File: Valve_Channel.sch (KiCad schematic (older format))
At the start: 12 parts, among them Q1 MMBT3904, Q2 Q_PMOS_GDS, U3 INA181AX

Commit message: added jtag programming header for uC
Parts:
- U3: symbol sternie:INA181AX -> bangbang_rev1-rescue:INA181AX-sternie
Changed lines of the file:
@@
 EESchema Schematic File Version 4
-LIBS:bangbang_rev1-cache
 EELAYER 30 0
 EELAYER END
@@
 $EndComp
 $Comp
-L sternie:INA181AX U3
+L bangbang_rev1-rescue:INA181AX-sternie U3
 U 1 1 59699268
 P 4750 4575

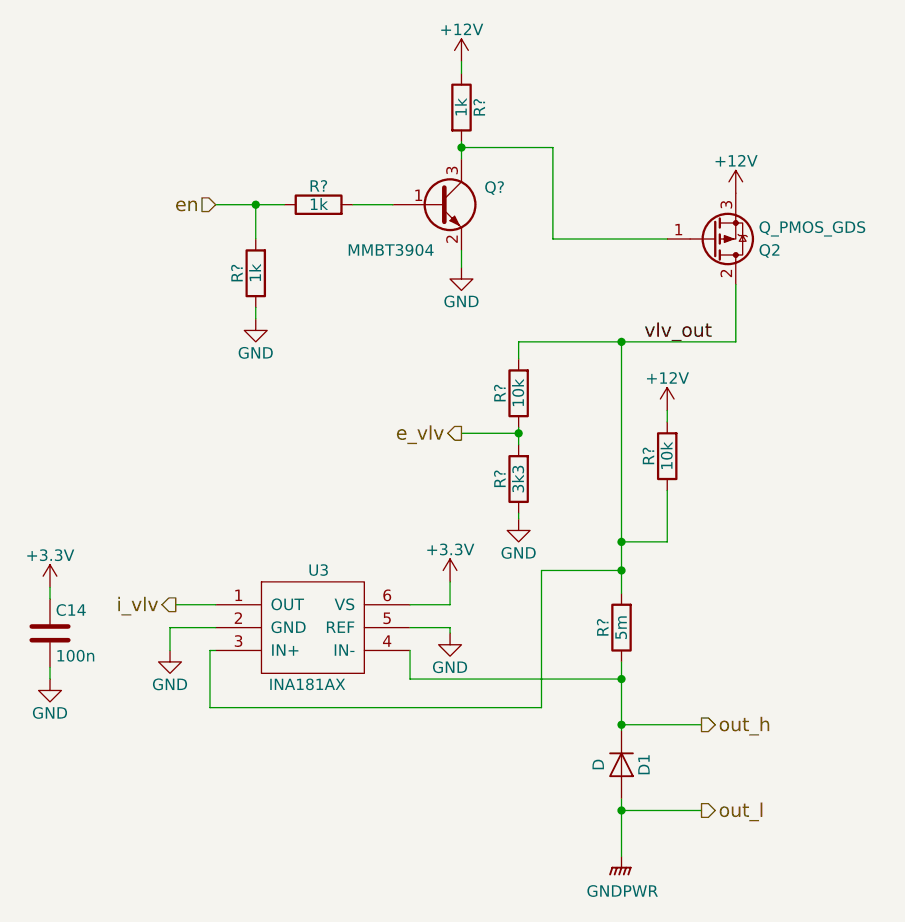
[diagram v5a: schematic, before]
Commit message: Eletrical Rules Check
Fixed some label names
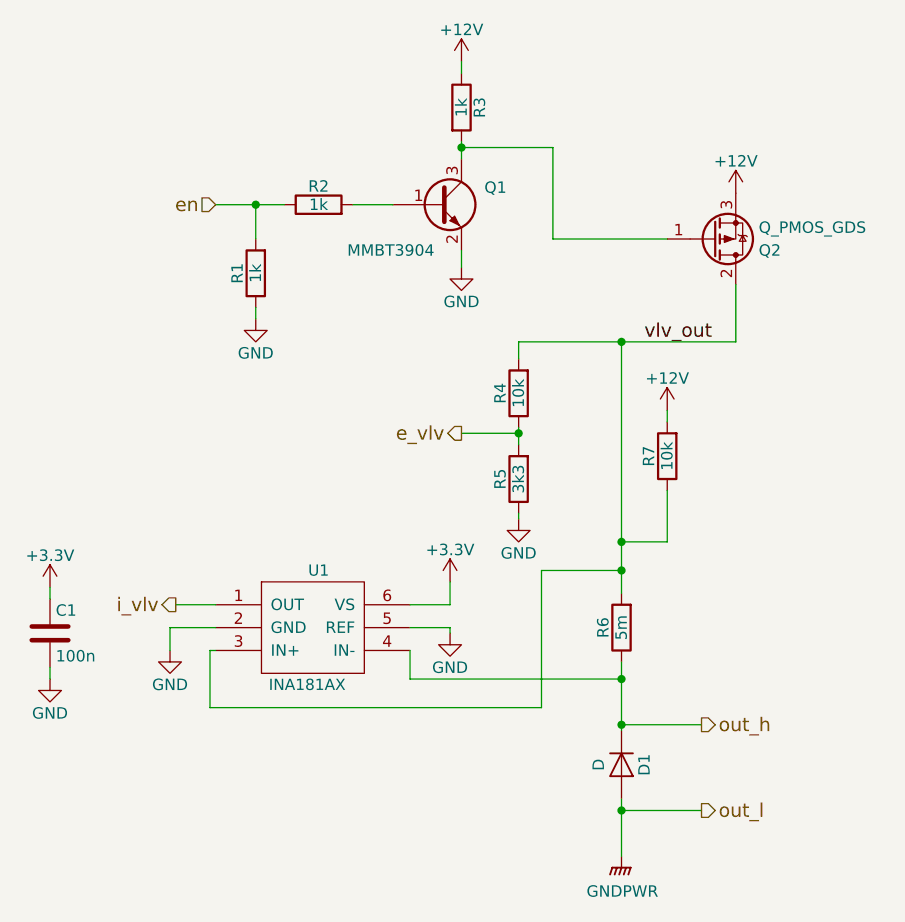
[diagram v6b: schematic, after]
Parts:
- renumbered C14 to C1, R2 to R1, R3 to R2, R4 to R3, R5 to R4, R6 to R5, R7 to R6, R8 to R7, U3 to U1

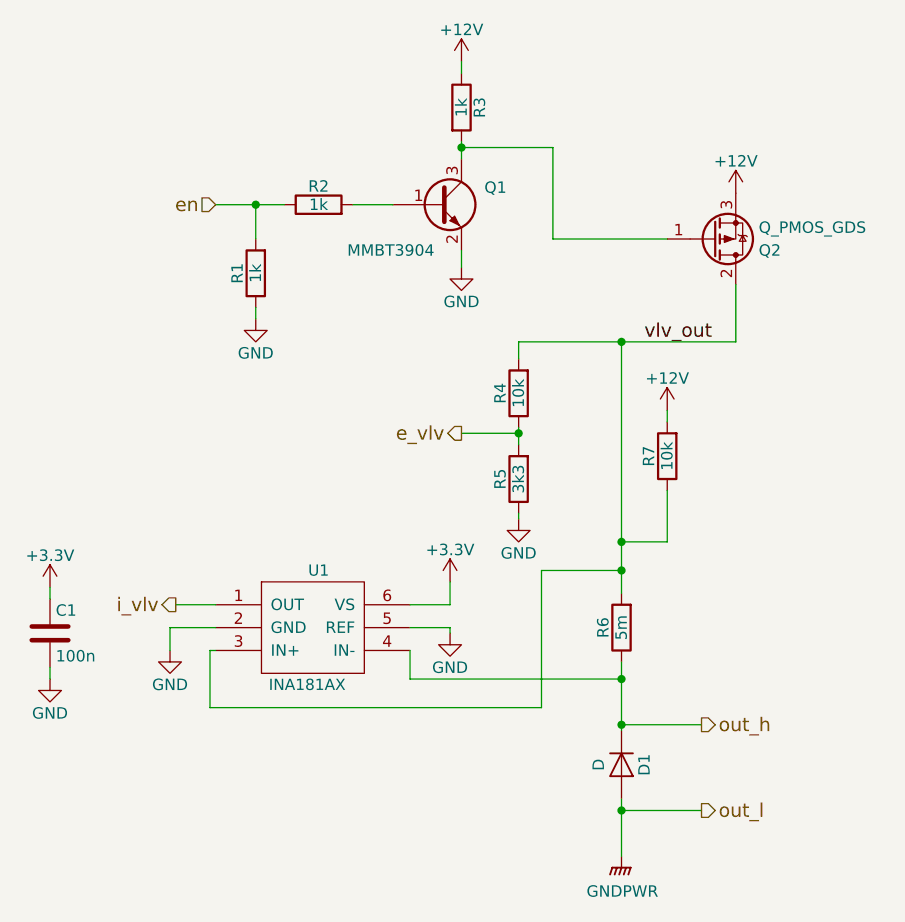
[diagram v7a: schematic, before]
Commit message: Motor Channel Cleanup
Removed some leftover labels in the motor channel after removal of the AND gate. Renumbering.
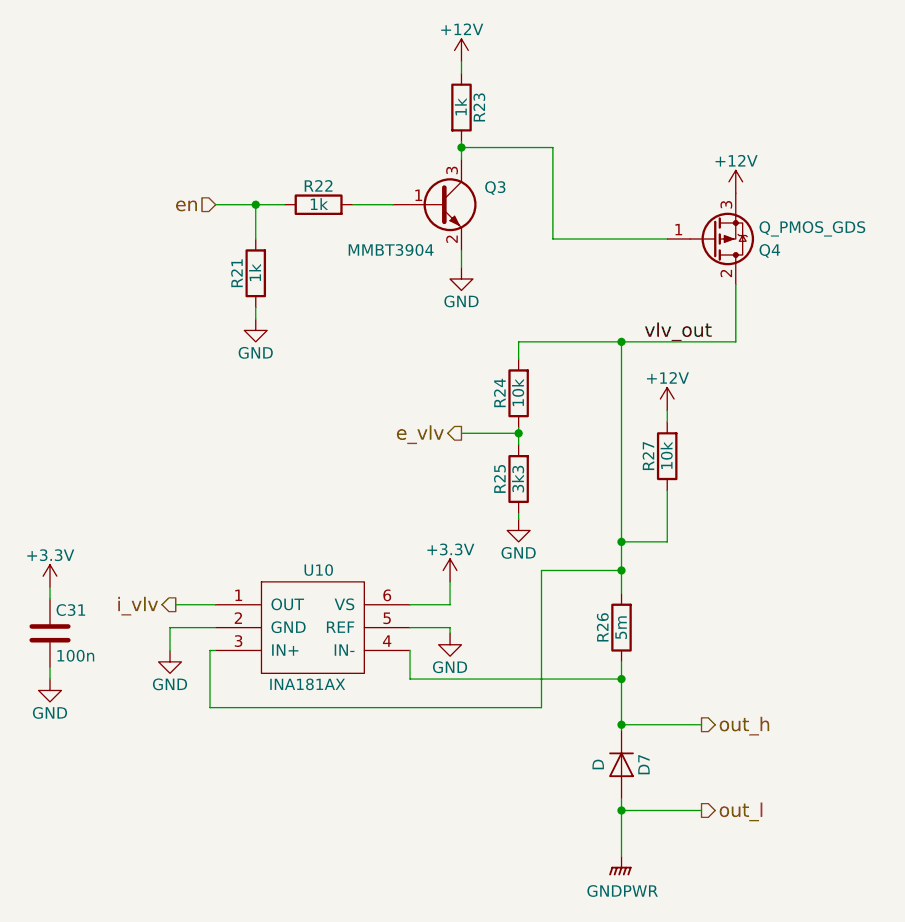
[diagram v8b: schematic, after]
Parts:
- renumbered C1 to C30, D1 to D6, R1 to R14, R2 to R15, R3 to R16, R4 to R17, R5 to R18, R6 to R19, R7 to R20, U1 to U9
